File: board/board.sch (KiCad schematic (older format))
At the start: 14 parts

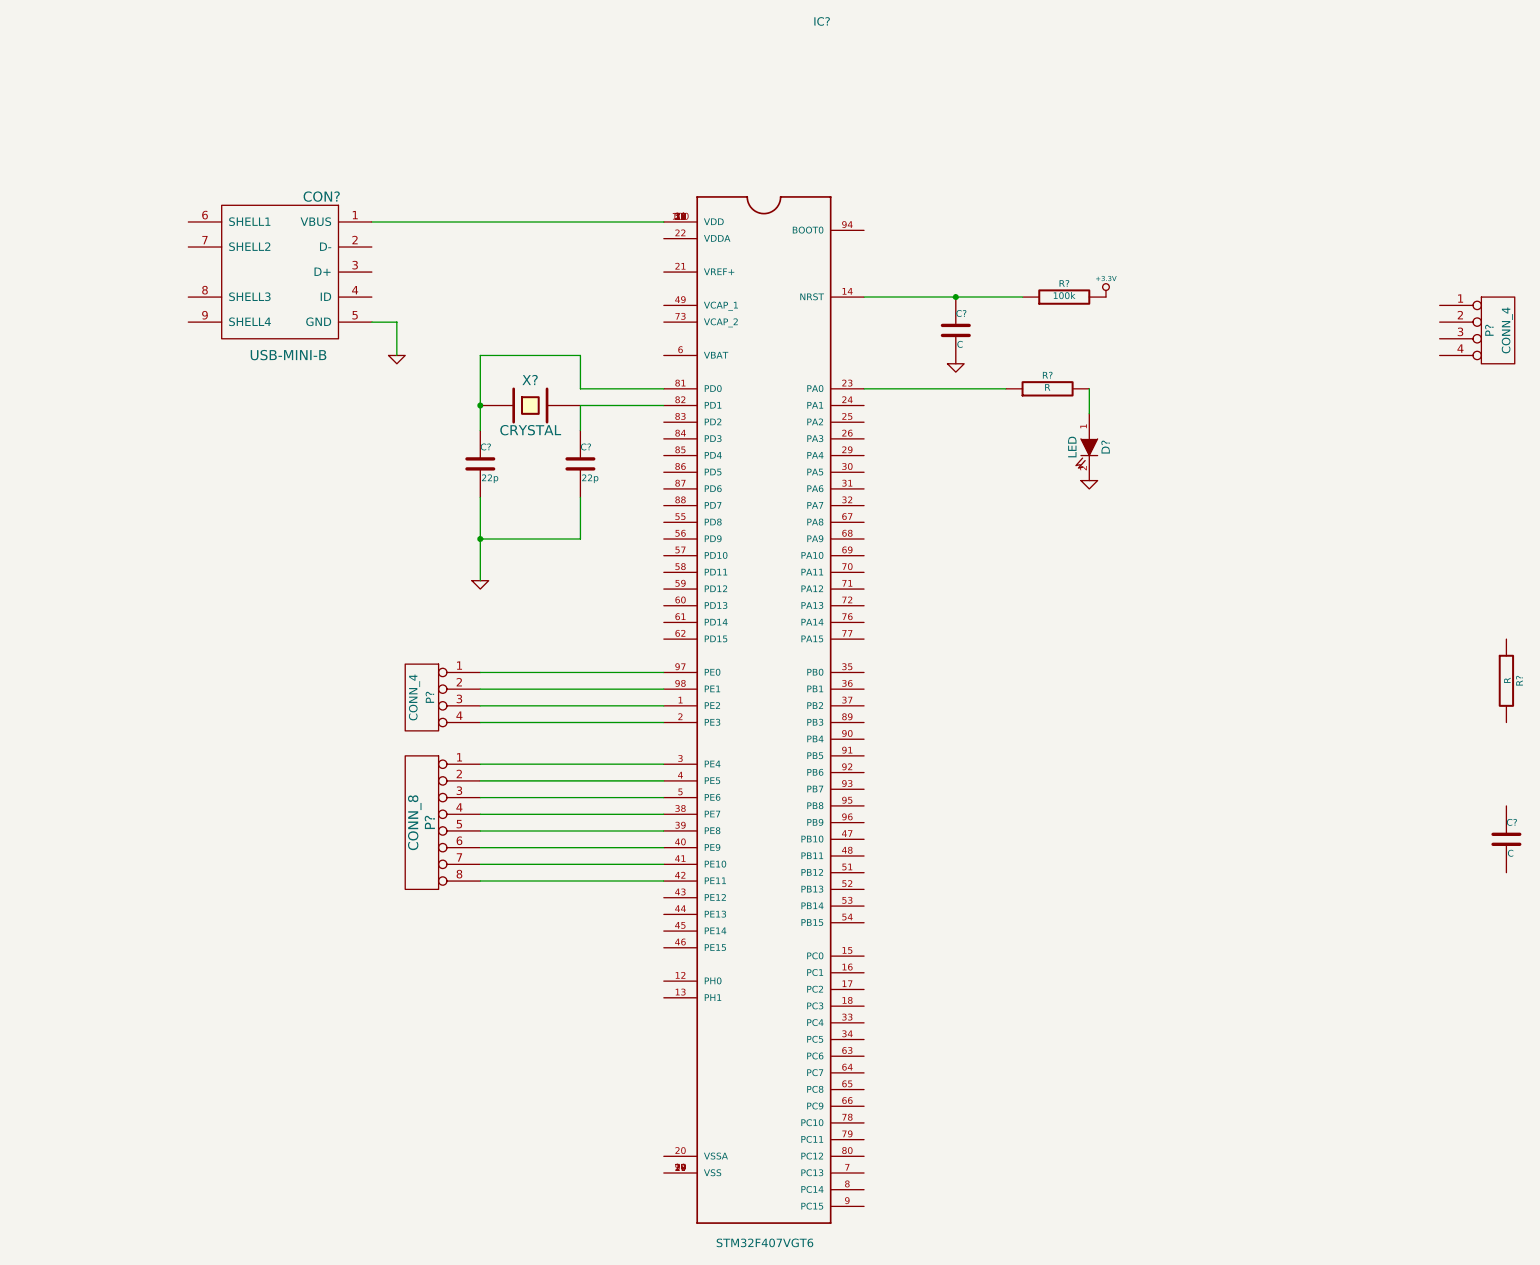
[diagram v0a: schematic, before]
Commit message: schematic update
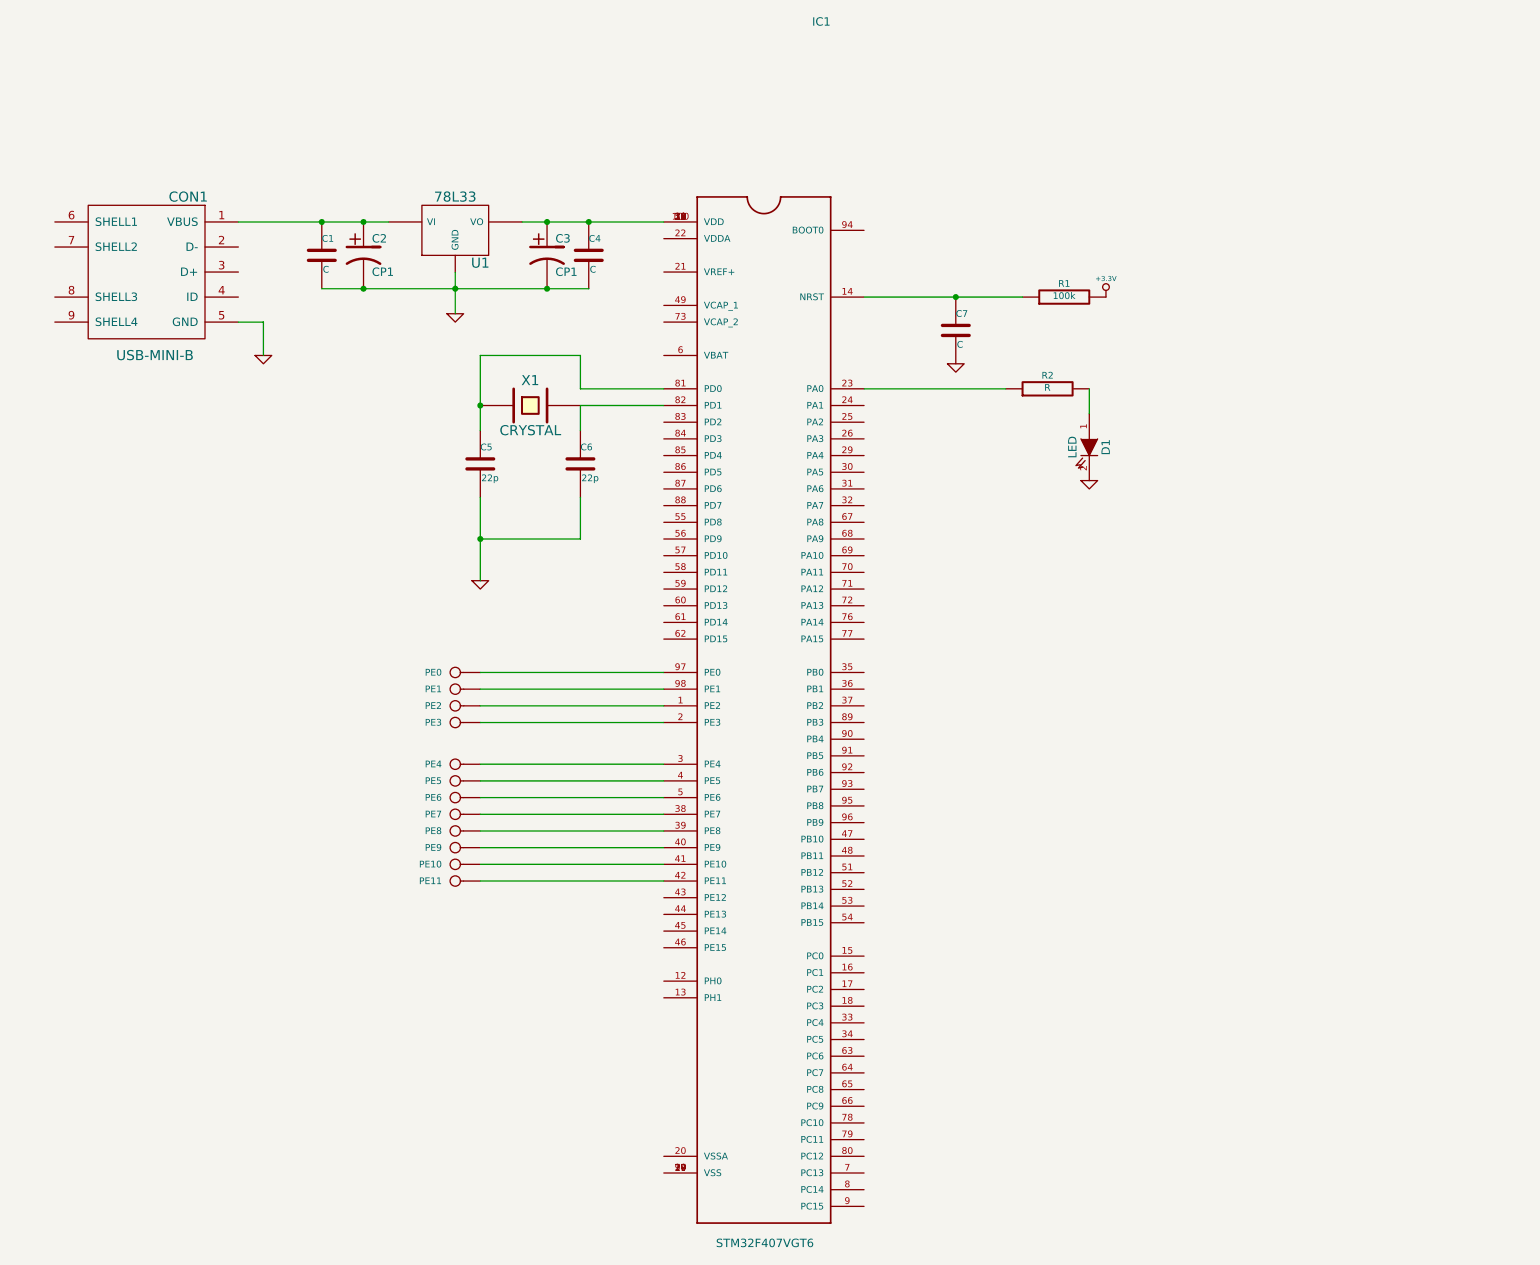
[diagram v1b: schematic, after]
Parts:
- removed C?: C, ~, symbol C
- removed P? (x2): CONN_4, ~, symbol CONN_4
- removed P?: CONN_8, ~, symbol CONN_8
- removed R?: R, ~, symbol R
- added C1, C4: C, ~, symbol C
- added C2, C3: CP1, ~, symbol CP1
- added PE0, PE1, PE10, PE11, PE2, PE3, PE4, PE5, PE6, PE7, PE8, PE9: CONN_1, ~, symbol CONN_1
- added U1: 78L33, ~, symbol 78L05
- gave numbers to parts that had none: 9
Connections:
- net GND: now also C1.2, C2.2, C3.2, C4.2, U1.GND
- net at IC1.1 (PE2): now also PE2.1
- net at IC1.100 (VDD), IC1.11 (VDD), IC1.19 (VDD)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: now also C3.1, C4.1, U1.VO; no longer CON1.1 (VBUS)
- net at IC1.2 (PE3): now also PE3.1
- net at IC1.3 (PE4): now also PE4.1
- net at IC1.38 (PE7): now also PE7.1
- net at IC1.39 (PE8): now also PE8.1
- net at IC1.4 (PE5): now also PE5.1
- net at IC1.40 (PE9): now also PE9.1
- net at IC1.41 (PE10): now also PE10.1
- net at IC1.42 (PE11): now also PE11.1
- net at IC1.5 (PE6): now also PE6.1
- net at IC1.97 (PE0): now also PE0.1
- net at IC1.98 (PE1): now also PE1.1
- new net: C1.1, C2.1, CON1.1 (VBUS), U1.VI
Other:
- moved on the sheet: CON1

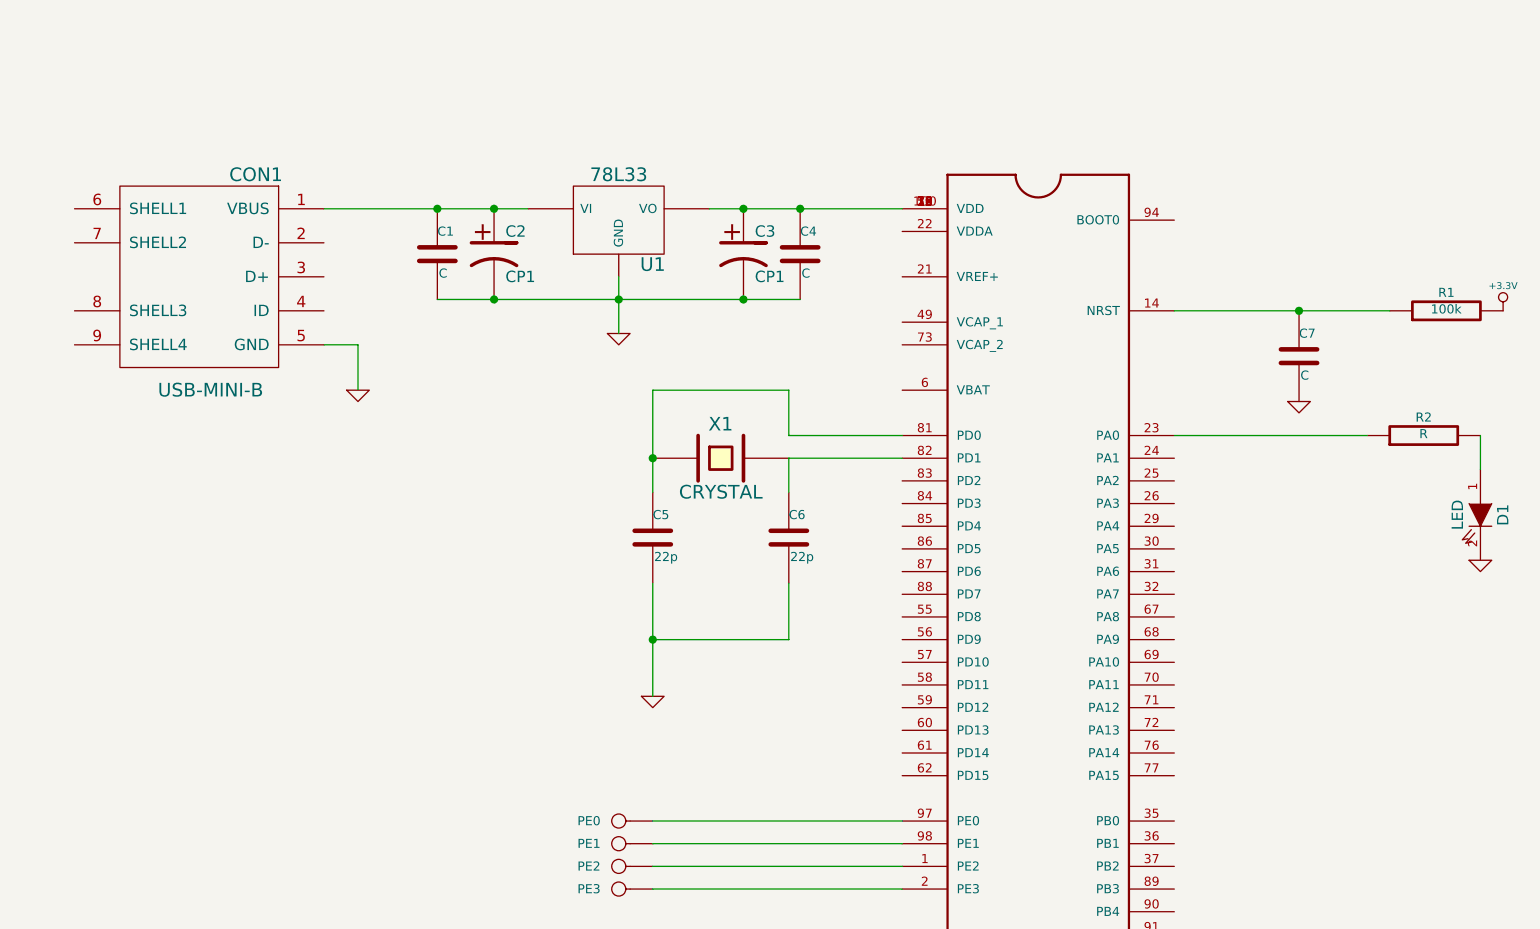
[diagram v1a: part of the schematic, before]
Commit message: added labels
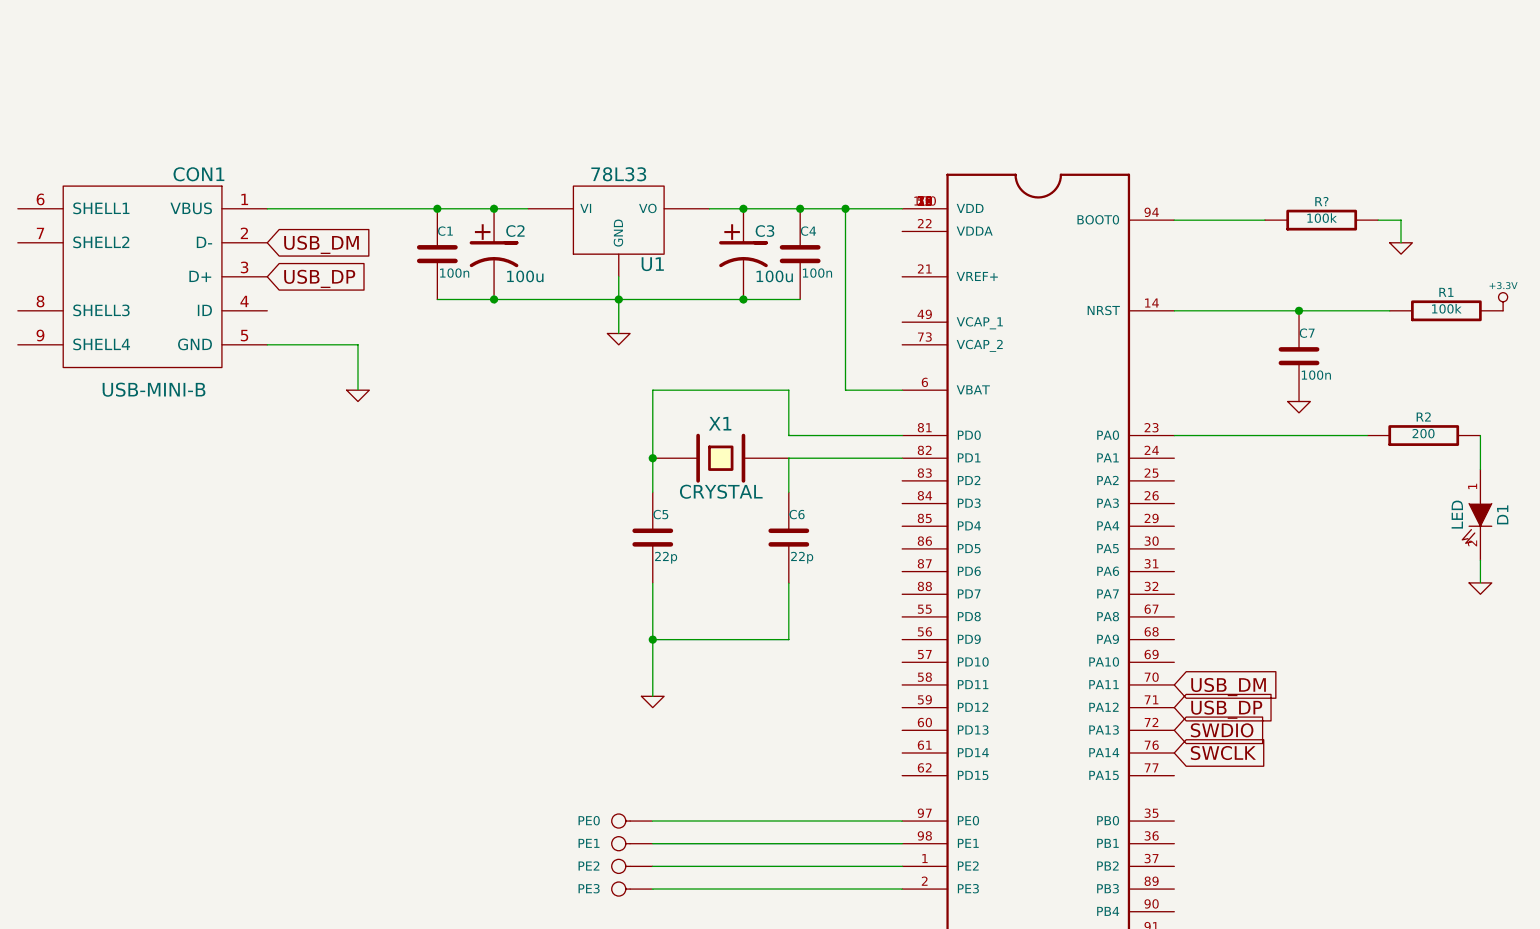
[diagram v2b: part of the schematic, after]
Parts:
- added R?: 100k, ~, symbol R
- C1, C4, C7: value C -> 100n
- C2, C3: value CP1 -> 100u
- R2: value R -> 200
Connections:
- net GND: now also R?.2
- net at C3.1, C4.1, IC1.100 (VDD)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: now also IC1.6 (VBAT)
- net USB_DM: now reaches IC1.70 (PA11)
- net USB_DM: now also CON1.2 (D-)
- net USB_DP: now reaches IC1.71 (PA12)
- net USB_DP: now also CON1.3 (D+)
- net SWDIO: now reaches IC1.72 (PA13)
- net SWCLK: now reaches IC1.76 (PA14)
- net at IC1.94 (BOOT0): now also R?.1
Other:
- moved on the sheet: CON1
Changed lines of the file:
@@
 Sheet 1 1
 Title ""
-Date "22 jan 2017"
+Date "23 jan 2017"
 Rev ""
 Comp ""
@@
 L USB-MINI-B CON1
 U 1 1 5883EC2D
-P 1500 1450
-F 0 "CON1" H 1250 1900 60  0000 C CNN
-F 1 "USB-MINI-B" H 1450 950 60  0000 C CNN
-F 2 "~" H 1500 1450 60  0000 C CNN
-F 3 "~" H 1500 1450 60  0000 C CNN
-	1    1500 1450
+P 1250 1450
+F 0 "CON1" H 1000 1900 60  0000 C CNN
+F 1 "USB-MINI-B" H 1200 950 60  0000 C CNN
+F 2 "~" H 1250 1450 60  0000 C CNN
+F 3 "~" H 1250 1450 60  0000 C CNN
+	1    1250 1450
 	-1   0    0    -1
 $EndComp
@@
 P 6350 1800
 F 0 "C7" H 6350 1900 40  0000 L CNN
-F 1 "C" H 6356 1715 40  0000 L CNN
+F 1 "100n" H 6356 1715 40  0000 L CNN
 F 2 "~" H 6388 1650 30  0000 C CNN
 F 3 "~" H 6350 1800 60  0000 C CNN
@@
 P 6900 2150
 F 0 "R2" V 6980 2150 40  0000 C CNN
-F 1 "R" V 6907 2151 40  0000 C CNN
+F 1 "200" V 6907 2151 40  0000 C CNN
 F 2 "~" V 6830 2150 30  0000 C CNN
 F 3 "~" H 6900 2150 30  0000 C CNN
@@
 L GND #PWR04
 U 1 1 58840BA4
-P 7150 2700
-F 0 "#PWR04" H 7150 2700 30  0001 C CNN
-F 1 "GND" H 7150 2630 30  0001 C CNN
-F 2 "" H 7150 2700 60  0000 C CNN
-F 3 "" H 7150 2700 60  0000 C CNN
-	1    7150 2700
+P 7150 2800
+F 0 "#PWR04" H 7150 2800 30  0001 C CNN
+F 1 "GND" H 7150 2730 30  0001 C CNN
+F 2 "" H 7150 2800 60  0000 C CNN
+F 3 "" H 7150 2800 60  0000 C CNN
+	1    7150 2800
 	1    0    0    -1
 $EndComp
@@
 $EndComp
 Wire Wire Line
-	2050 1750 2200 1750
+	1800 1750 2200 1750
 Wire Wire Line
 	2200 1750 2200 1950
@@
 P 2550 1350
 F 0 "C1" H 2550 1450 40  0000 L CNN
-F 1 "C" H 2556 1265 40  0000 L CNN
+F 1 "100n" H 2556 1265 40  0000 L CNN
 F 2 "~" H 2588 1200 30  0000 C CNN
 F 3 "~" H 2550 1350 60  0000 C CNN
@@
 P 4150 1350
 F 0 "C4" H 4150 1450 40  0000 L CNN
-F 1 "C" H 4156 1265 40  0000 L CNN
+F 1 "100n" H 4156 1265 40  0000 L CNN
 F 2 "~" H 4188 1200 30  0000 C CNN
 F 3 "~" H 4150 1350 60  0000 C CNN
@@
 P 2800 1350
 F 0 "C2" H 2850 1450 50  0000 L CNN
-F 1 "CP1" H 2850 1250 50  0000 L CNN
+F 1 "100u" H 2850 1250 50  0000 L CNN
 F 2 "~" H 2800 1350 60  0000 C CNN
 F 3 "~" H 2800 1350 60  0000 C CNN
@@
 P 3900 1350
 F 0 "C3" H 3950 1450 50  0000 L CNN
-F 1 "CP1" H 3950 1250 50  0000 L CNN
+F 1 "100u" H 3950 1250 50  0000 L CNN
 F 2 "~" H 3900 1350 60  0000 C CNN
 F 3 "~" H 3900 1350 60  0000 C CNN
@@
 Connection ~ 3900 1550
 Wire Wire Line
-	2050 1150 2950 1150
+	1800 1150 2950 1150
 Connection ~ 2550 1150
 Connection ~ 2800 1150
@@
 Connection ~ 3900 1150
 Connection ~ 4150 1150
+Wire Wire Line
+	4600 1950 4350 1950
+Wire Wire Line
+	4350 1950 4350 1150
+Connection ~ 4350 1150
+$Comp
+L R R?
+U 1 1 588581F9
+P 6450 1200
+F 0 "R?" V 6530 1200 40  0000 C CNN
+F 1 "100k" V 6457 1201 40  0000 C CNN
+F 2 "~" V 6380 1200 30  0000 C CNN
+F 3 "~" H 6450 1200 30  0000 C CNN
+	1    6450 1200
+	0    -1   -1   0
+$EndComp
+Wire Wire Line
+	5800 1200 6200 1200
+$Comp
+L GND #PWR?
+U 1 1 5885822C
+P 6800 1300
+F 0 "#PWR?" H 6800 1300 30  0001 C CNN
+F 1 "GND" H 6800 1230 30  0001 C CNN
+F 2 "" H 6800 1300 60  0000 C CNN
+F 3 "" H 6800 1300 60  0000 C CNN
+	1    6800 1300
+	1    0    0    -1
+$EndComp
+Wire Wire Line
+	6700 1200 6800 1200
+Wire Wire Line
+	6800 1200 6800 1300
+Wire Wire Line
+	7150 2700 7150 2800
+Text GLabel 1800 1300 2    60   Input ~ 0
+USB_DM
+Text GLabel 1800 1450 2    60   Input ~ 0
+USB_DP
+Text GLabel 5800 3250 2    60   Input ~ 0
+USB_DM
+Text GLabel 5800 3350 2    60   Input ~ 0
+USB_DP
+Text GLabel 5800 3450 2    60   Input ~ 0
+SWDIO
+Text GLabel 5800 3550 2    60   Input ~ 0
+SWCLK
 $EndSCHEMATC

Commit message: pcb
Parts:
- gave numbers to parts that had none: 1
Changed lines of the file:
@@
 Connection ~ 4350 1150
 $Comp
-L R R?
+L R R3
 U 1 1 588581F9
 P 6450 1200
-F 0 "R?" V 6530 1200 40  0000 C CNN
+F 0 "R3" V 6530 1200 40  0000 C CNN
 F 1 "100k" V 6457 1201 40  0000 C CNN
 F 2 "~" V 6380 1200 30  0000 C CNN
@@
 	5800 1200 6200 1200
 $Comp
-L GND #PWR?
+L GND #PWR07
 U 1 1 5885822C
 P 6800 1300
-F 0 "#PWR?" H 6800 1300 30  0001 C CNN
+F 0 "#PWR07" H 6800 1300 30  0001 C CNN
 F 1 "GND" H 6800 1230 30  0001 C CNN
 F 2 "" H 6800 1300 60  0000 C CNN
